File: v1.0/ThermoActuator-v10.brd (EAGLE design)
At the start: 100 x 80 mm, 58 parts, among them IC1 LM358D, IC2 ULN2003AD, IC3 LM358D

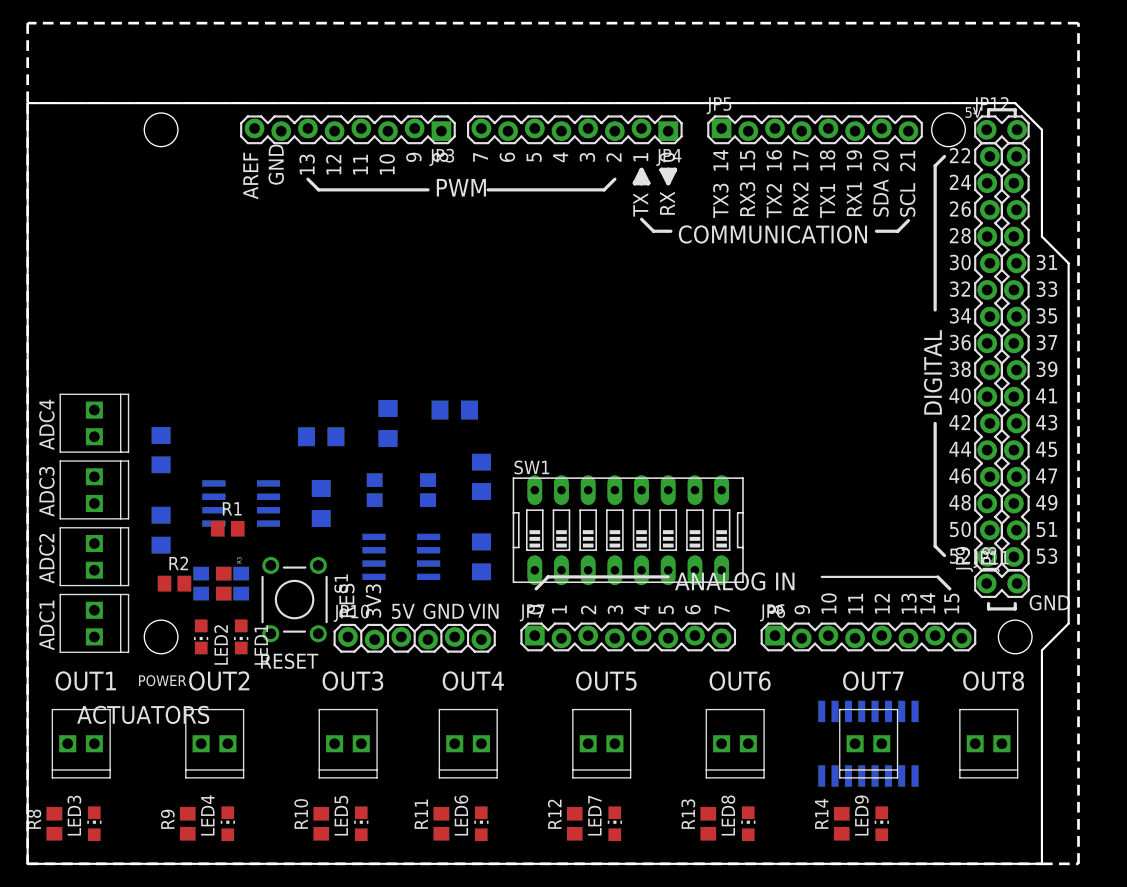
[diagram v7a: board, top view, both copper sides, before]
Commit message: all channels laid out
somewhat inconsistent but all elements
laid out except the button
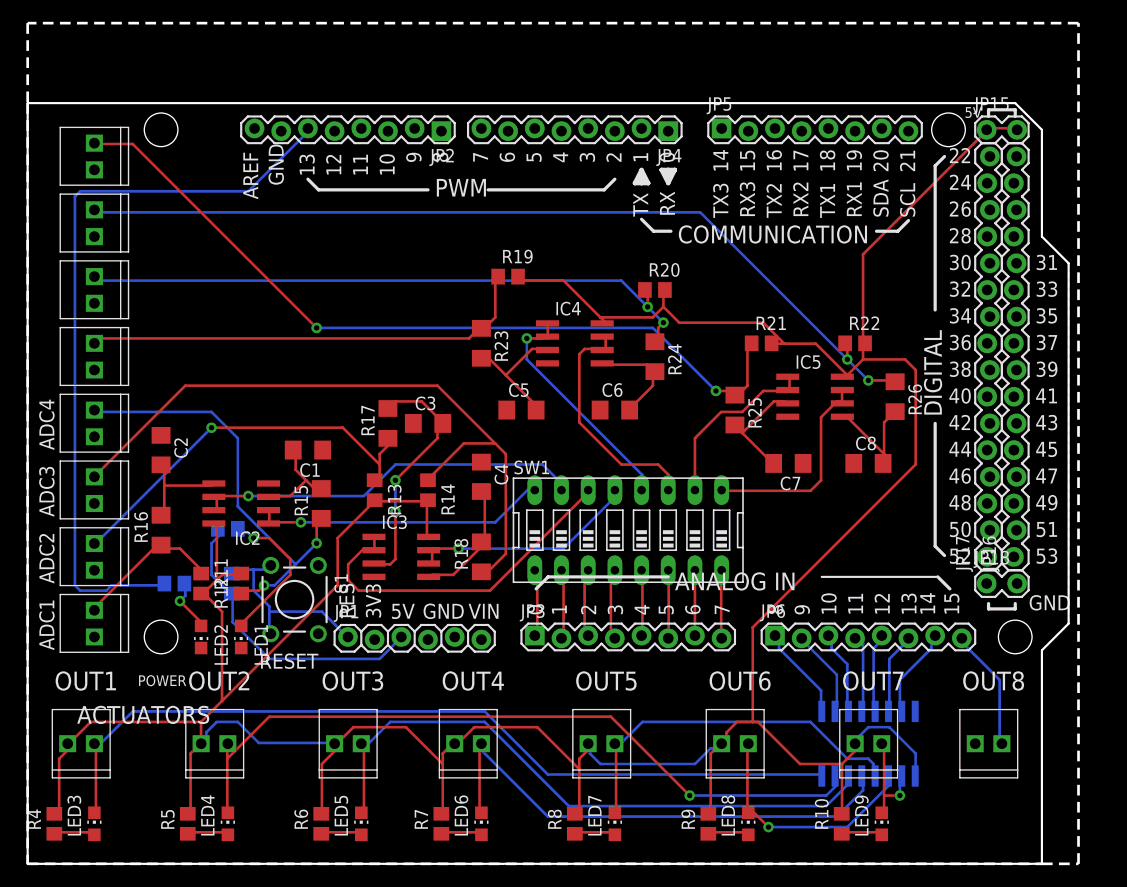
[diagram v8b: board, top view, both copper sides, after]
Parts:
- added C5, C6, C7, C8: 10nF, rcl:C1206
- added IC4, IC5: LM358D, linear:SO08
- added JP1: (no value), SparkFun:1X06_LOCK
- added JP24, JP25, JP26: (no value), SparkFun-Connectors:1X02_2.54_SCREWTERM
- added R19, R20, R21, R22: 100K, rcl:R0805
- added R23, R24, R25, R26: 10K, rcl:R1206
- IC1: value LM358D -> ULN2003AD; device linear:SO08 -> uln-udn:SO16
- IC2: value ULN2003AD -> LM358D; device uln-udn:SO16 -> linear:SO08
- JP10: device SparkFun:1X06_LOCK -> SparkFun-Connectors:1X02_2.54_SCREWTERM
- JP11, JP12: device SparkFun:1X02_LOCK -> SparkFun-Connectors:1X02_2.54_SCREWTERM
- JP13, JP19, JP20, JP21, JP22, JP23: value ADC2 -> (none)
- JP14: value OUT1 -> (none)
- JP15: value OUT2 -> (none); device SparkFun-Connectors:1X02_2.54_SCREWTERM -> SparkFun:1X02_LOCK
- JP16, JP17: value ADC2 -> M16LOCK; device SparkFun-Connectors:1X02_2.54_SCREWTERM -> SparkFun:1X16_LOCK
- JP18: value ADC2 -> (none); device SparkFun-Connectors:1X02_2.54_SCREWTERM -> SparkFun:1X02_LOCK
- JP2: value ADC1 -> (none); device SparkFun-Connectors:1X02_2.54_SCREWTERM -> SparkFun:1X08_LOCK
- JP7: device SparkFun:1X08_LOCK -> SparkFun-Connectors:1X02_2.54_SCREWTERM
- JP8, JP9: value M16LOCK -> (none); device SparkFun:1X16_LOCK -> SparkFun-Connectors:1X02_2.54_SCREWTERM
- R1: value 330 -> (none)
- R11, R12, R13, R14: value 330 -> 100K
- R15, R17: value 100K -> 10K; device rcl:R0805 -> rcl:R1206
- R3: value (none) -> 330
- R4, R6: value 100K -> 330
- R5, R7: value 10K -> 330; device rcl:R1206 -> rcl:R0805
- moved JP15 93.0 mm to (91.4, 69.8), turned to 0 degrees
- moved JP21 88.4 mm to (6.35, 30.5), turned to 270 degrees
- moved JP14 86.4 mm to (92.7, 11.4)
- moved JP8 77.0 mm to (19.1, 11.4), turned to 180 degrees
- moved JP13 76.0 mm to (81.3, 11.4), turned to 180 degrees
- moved JP20 76.0 mm to (6.35, 24.1), turned to 270 degrees
- moved JP19 69.9 mm to (6.35, 43.2), turned to 270 degrees
- moved JP16 64.7 mm to (94.0, 29.2), turned to 90 degrees
- moved IC1 63.9 mm to (80.0, 11.4), turned to 180 degrees
- moved IC2 63.9 mm to (20.3, 34.3), flipped to the top, turned to 90 degrees
- moved JP12 62.7 mm to (68.6, 11.4), turned to 180 degrees
- moved JP9 62.3 mm to (31.8, 11.4), turned to 180 degrees
- moved JP17 51.4 mm to (91.4, 29.2), turned to 90 degrees
- moved R14 50.6 mm to (38.1, 35.6), turned to 270 degrees
- moved R10 49.5 mm to (77.5, 3.81)
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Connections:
- new net AS4: IC4.1, IC4.2, SW1.12
- new net AS5: IC4.6, IC4.7, SW1.11
- new net AS6: IC5.1, IC5.2, SW1.10
- new net AS7: IC5.6, IC5.7, SW1.9
- new net N$24: JP23.P2, R19.1, R23.1
- new net N$25: C5.2, IC4.3, R23.2
- new net N$26: JP24.P2, R20.1, R24.1
- new net N$27: C6.2, IC4.5, R24.2
- new net N$28: JP25.P2, R21.1, R25.1
- new net N$29: C7.2, IC5.3, R25.2
- new net N$30: JP26.P2, R22.1, R26.1
- new net N$31: C8.2, IC5.5, R26.2
- net 3.3: now also JP1.2; no longer JP10.2
- net 5V: now also JP1.3, R2.2; no longer JP10.3, R3.2
- net A10: now also IC1.3; no longer IC2.3
- net A11: now also IC1.4; no longer IC2.4
- net A12: now also IC1.5; no longer IC2.5
- net A13: now also IC1.6; no longer IC2.6
- net A14: now also IC1.7; no longer IC2.7
- net A8: now also IC1.1; no longer IC2.1
- net A9: now also IC1.2; no longer IC2.2
- net AO0: now also IC1.16, JP7.P2; no longer IC2.16, JP14.P2
- net AO1: now also IC1.15, JP8.P2; no longer IC2.15, JP15.P2
- net AO2: now also IC1.14, JP9.P2; no longer IC2.14, JP16.P2
- net AO3: now also IC1.13, JP10.P2; no longer IC2.13, JP17.P2
- net AO4: now also IC1.12, JP11.P2; no longer IC2.12, JP18.P2
- net AO5: now also IC1.11, JP12.P2; no longer IC2.11, JP19.P2
- net AO6: now also IC1.10, JP13.P2; no longer IC2.10, JP20.P2
- net AO7: now also JP14.P2; no longer JP21.P2
- net AREF: now also JP2.8; no longer JP3.8
- net AS0: now also IC2.1, IC2.2; no longer IC1.1, IC1.2
- net AS1: now also IC2.6, IC2.7; no longer IC1.6, IC1.7
- net D10: now also JP2.3; no longer JP3.3
- net D11: now also JP2.4; no longer JP3.4
- net D12: now also JP2.5; no longer JP3.5
- net D13: now also JP2.6, R3.2; no longer JP3.6, R2.2
- net D22: now also JP17.1; no longer JP9.1
- net D23: now also JP16.16; no longer JP8.16
- net D24: now also JP17.2; no longer JP9.2
- net D25: now also JP16.15; no longer JP8.15
- net D26: now also JP17.3; no longer JP9.3
- net D27: now also JP16.14; no longer JP8.14
- net D28: now also JP17.4; no longer JP9.4
- net D29: now also JP16.13; no longer JP8.13
- net D30: now also JP17.5; no longer JP9.5
- net D31: now also JP16.12; no longer JP8.12
- net D32: now also JP17.6; no longer JP9.6
- net D33: now also JP16.11; no longer JP8.11
- net D34: now also JP17.7; no longer JP9.7
- net D35: now also JP16.10; no longer JP8.10
- net D36: now also JP17.8; no longer JP9.8
- net D37: now also JP16.9; no longer JP8.9
- net D38: now also JP17.9; no longer JP9.9
- net D39: now also JP16.8; no longer JP8.8
- net D40: now also JP17.10; no longer JP9.10
- net D41: now also JP16.7; no longer JP8.7
- net D42: now also JP17.11; no longer JP9.11
- net D43: now also JP16.6; no longer JP8.6
- net D44: now also JP17.12; no longer JP9.12
- net D45: now also JP16.5; no longer JP8.5
- net D46: now also JP17.13; no longer JP9.13
- net D47: now also JP16.4; no longer JP8.4
- net D48: now also JP17.14; no longer JP9.14
- net D49: now also JP16.3; no longer JP8.3
- net D50: now also JP17.15; no longer JP9.15
- net D51: now also JP16.2; no longer JP8.2
- net D52: now also JP17.16; no longer JP9.16
- net D53: now also JP16.1; no longer JP8.1
- net D8: now also JP2.1; no longer JP3.1
- net D9: now also JP2.2; no longer JP3.2
- net GND: now also C5.1, C6.1, C7.1, C8.1, IC1.8, IC2.4, IC4.4, IC5.4, JP1.4, JP1.5, JP14.P1, JP18.1, JP18.2, JP19.P1, JP2.7, JP20.P1, JP24.P1, JP25.P1, JP26.P1; no longer IC1.4, IC2.8, JP10.4, JP10.5, JP11.1, JP11.2, JP13.P1, JP2.P1, JP3.7
- net N$1: now also JP19.P2, R11.1, R15.1; no longer JP2.P2, R4.1, R5.1
- net N$10: now also JP3.8; no longer JP7.8
- net N$11: now also JP20.P2, R12.1, R16.1; no longer JP13.P2, R6.1, R7.1
- net N$12: now also IC2.5, R16.2; no longer IC1.5, R7.2
- net N$126: now also R2.1; no longer R1.1
- net N$127: now also R3.1; no longer R2.1
- net N$13: now also R4.1; no longer R8.1
- net N$14: now also R5.1; no longer R9.1
- net N$15: now also R6.1; no longer R10.1
- net N$16: now also R7.1; no longer R11.1
- net N$17: now also R8.1; no longer R12.1
- net N$18: now also R9.1; no longer R13.1
- net N$19: now also R10.1; no longer R14.1
- net N$2: now also IC2.3, R15.2; no longer IC1.3, R5.2
- net N$20: now also JP21.P2, R13.1, R17.1; no longer JP22.P2, R15.1, R16.1
- net N$21: now also R17.2; no longer R16.2
- net N$22: now also JP22.P2, R14.1; no longer JP23.P2, R17.1
- net N$3: now also JP3.1; no longer JP7.1
- net N$4: now also JP3.2; no longer JP7.2
- net N$5: now also JP3.3; no longer JP7.3
- net N$6: now also JP3.4; no longer JP7.4
- net N$7: now also JP3.5; no longer JP7.5
- net N$8: now also JP3.6; no longer JP7.6
- net N$9: now also JP3.7; no longer JP7.7
- net RES: now also JP1.1, R1.1; no longer JP10.1, R3.1
- net VDD: now also IC1.9, IC2.8, IC4.8, IC5.8, JP10.P1, JP11.P1, JP12.P1, JP13.P1, JP15.1, JP15.2, JP7.P1, JP8.P1, JP9.P1, R19.2, R20.2, R21.2, R22.2, R5.2, R7.2; no longer IC1.8, IC2.9, JP12.1, JP12.2, JP14.P1, JP15.P1, JP16.P1, JP17.P1, JP18.P1, JP19.P1, JP20.P1, R15.2, R17.2
- net VIN: now also JP1.6; no longer JP10.6
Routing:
- net VDD: track 0.00 -> 324.2 mm
- net N$30: track 0.00 -> 84.8 mm, vias 0 -> 2
- net AO0: track 0.00 -> 80.2 mm
- net N$28: track 0.00 -> 76.9 mm, vias 0 -> 2
- net D13: track 0.00 -> 71.1 mm
- net AO1: track 0.00 -> 70.7 mm, vias 0 -> 1
- net N$22: track 0.00 -> 66.1 mm
- net N$26: track 0.00 -> 60.0 mm, vias 0 -> 2
- net AO2: track 0.00 -> 59.3 mm
- net AO3: track 0.00 -> 48.8 mm
- net N$24: track 0.00 -> 43.3 mm
- net N$1: track 0.00 -> 40.8 mm, vias 0 -> 2
- net N$20: track 0.00 -> 37.8 mm, vias 0 -> 1
- net AS1: track 0.00 -> 37.7 mm, vias 0 -> 1
- net AO4: track 0.00 -> 35.5 mm
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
